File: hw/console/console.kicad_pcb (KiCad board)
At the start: 2 copper layers, 156 x 74 mm, 161 parts, among them J1 Batt, J301 USB-C 16P, J401 DM3AT-SF-PEJM5, J501 SPK 8R, J601 FFC-40 0.5mm, J901 UART, Q601 AO3400A, SW1 Движок, SW101 UP, SW102 DOWN, SW103 LEFT, SW104 RIGHT, SW105 SELECT, SW106 START, SW107 A, SW108 B, SW109 C, SW110 D, U1 F133-A, U2 SY8089AAAC, U3 SY8089AAAC, U4 SY8089AAAC, U401 W25Q32JVSSIQ, U5 TP4056, U501 PAM8301, Y1 24 МГц, Y2 32.768 кГц

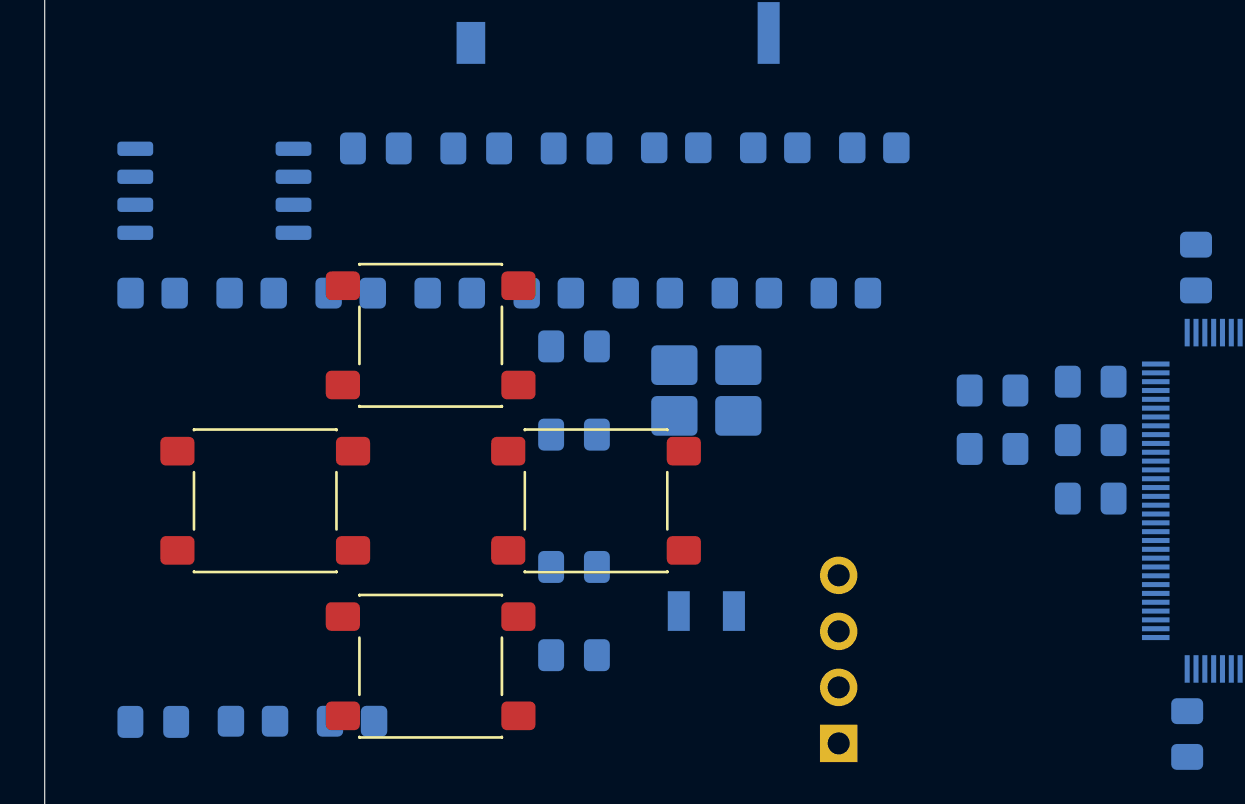
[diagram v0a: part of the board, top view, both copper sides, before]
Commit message: hw: осмотр платы глазами — флешка и кварцы стояли у края, а не у своих выводов
Проверки давали ноль, картинка — нет. Свободный карман вплотную к левому
торцу корпуса никто не занял, и обе детали, которым положено быть ближе всех,
оказались у самого края платы:

  U401 SPI NOR — 40 мм до выводов 14…19, хотя рядом с ними было пусто;
  Y1 24 МГц и Y2 32.768 кГц — по 20 мм до выводов 21…25.

Причина в том, что кольцо развязки занимает на левой стороне y = 32…36 в двух
рядах, а раскладчик по зонам просто ставил детали в свою зону у края. Теперь
U401 сидит в кармане y = 37…43 прямо у корпуса, кварцы — напротив своих
выводов за кольцом. Приоритет у развязки: петля тока по питанию важнее длины
кварцевой дорожки, а 24 МГц спокойно терпит десяток миллиметров.

Проверка на кварцы это пропускала, потому что порог «далеко» я поставил 25 мм
с потолка — при том, что вся левая сторона корпуса 12 мм в длину. Порог 12,
и заведена такая же проверка для флешки. Проверок стало восемнадцать.

Заодно 05-audio.md §7.5.1: выход класса D фильтрлесс, между усилителем и
динамиком катушек нет, и пара OUT+/OUT- — самый шумный узел платы. Требование
на разводку записано: вести парой, одинаковой длины, ничего чувствительного
рядом; если станет тесно — двигать U501 к разъёму, а не растягивать пару.

18 проверок платы — ноль, DRC кроме неразведённого — ноль, конвейер
идемпотентен, схема ERC ноль и audit.py ноль.

Co-Authored-By: Claude Opus 5 <noreply@anthropic.com>
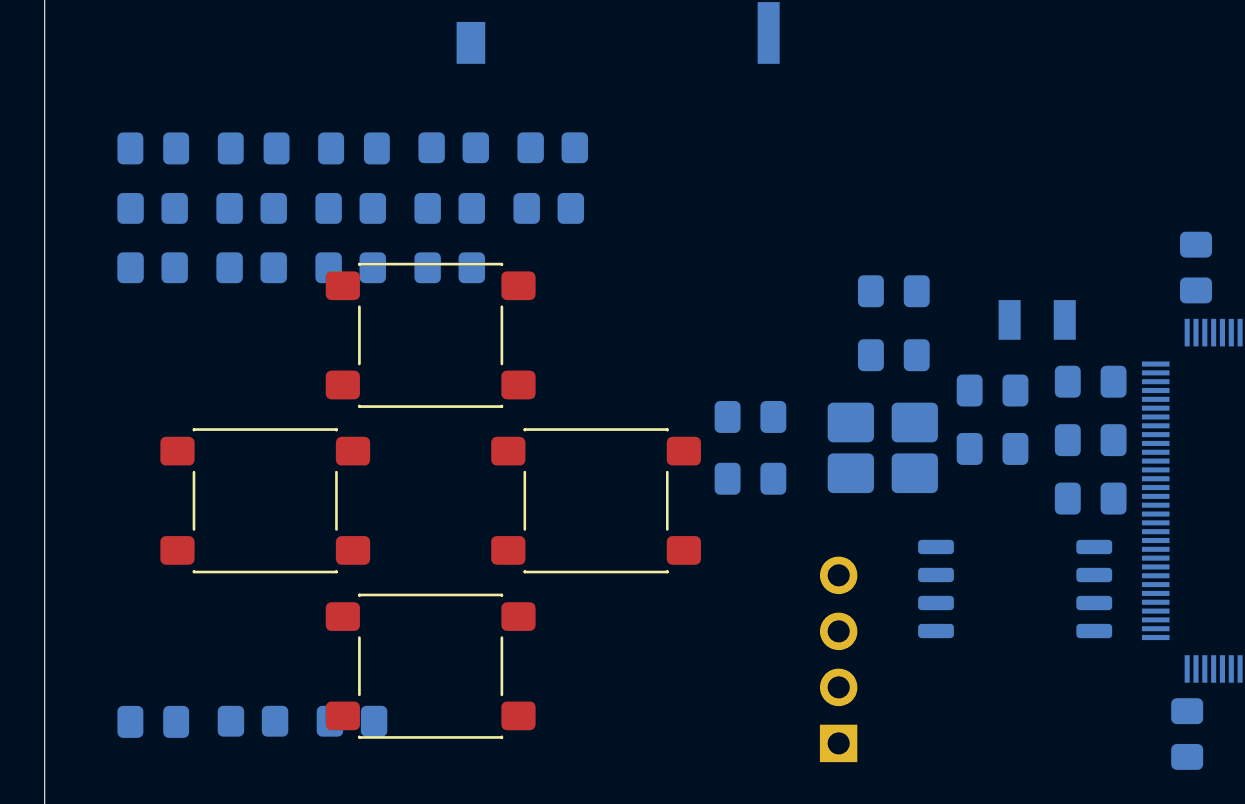
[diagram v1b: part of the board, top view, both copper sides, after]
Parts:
- moved U401 40.5 mm to (94.0, 81.0)
- moved R403 32.8 mm to (54.9, 63.7)
- moved Y2 20.0 mm to (95.0, 68.8)
- moved C18 19.9 mm to (88.5, 70.4)
- moved C17 19.1 mm to (88.5, 67.5)
- moved R411 18.0 mm to (68.4, 66.4)
- moved R408 18.0 mm to (54.9, 66.4)
- moved R409 18.0 mm to (59.4, 66.4)
- moved R410 18.0 mm to (63.9, 66.4)
- moved C401 10.1 mm to (54.9, 61.0)
- moved R401 10.1 mm to (68.5, 61.0)
- moved R402 10.1 mm to (73.0, 61.0)
- moved C402 10.1 mm to (59.5, 61.0)
- moved C403 10.1 mm to (64.0, 61.0)
- moved C15 8.62 mm to (82.0, 73.2)
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
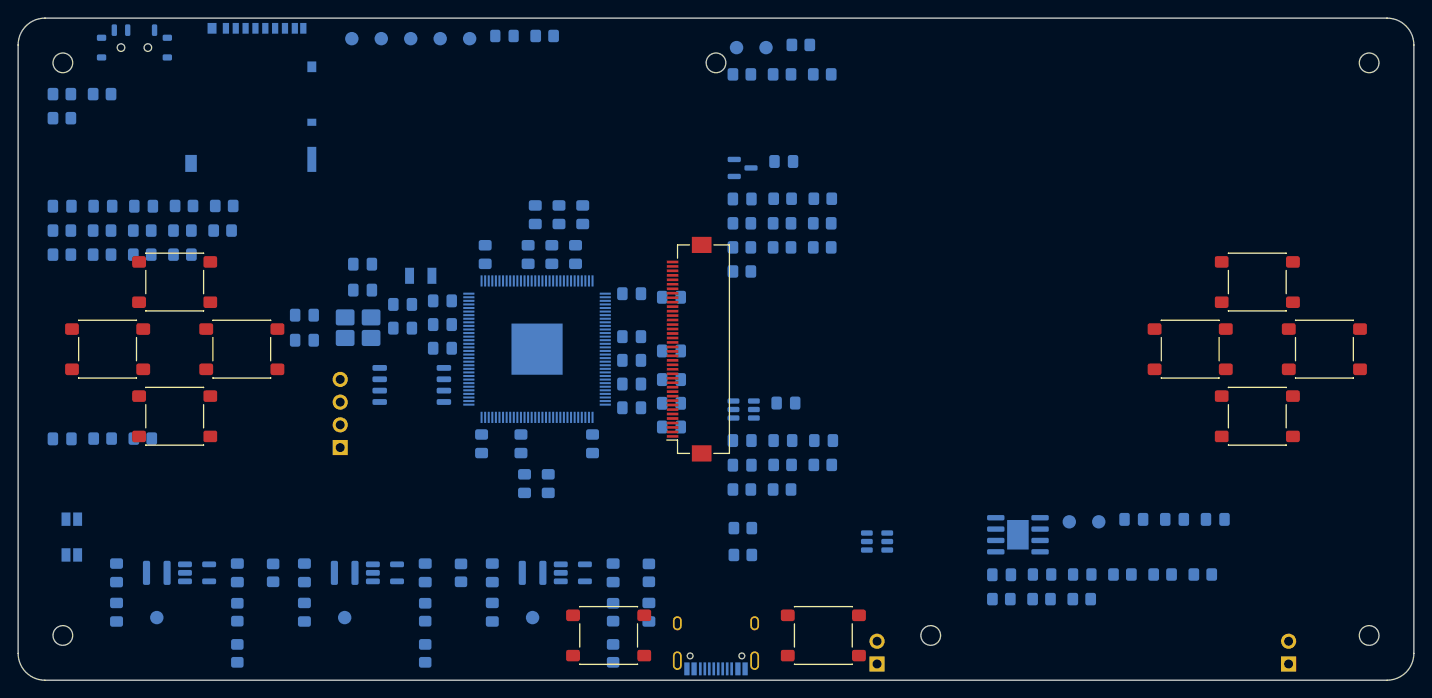
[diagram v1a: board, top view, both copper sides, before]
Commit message: hw: вариант C — все детали на лице, изнанка отдана банке
Andrey заметил то, что я проглядел: разъём шлейфа стоял на лице, а F133 на
изнанке. Посчитал по плате — 36 цепей требовали перехода через слой, и все в
самом тесном месте: шаг площадок разъёма 0.5 мм, наша переходная с зазором
даёт 1.1, сорок штук в ряд заняли бы 44 мм при ширине разъёма 19.5. То есть
три ряда веером и 36 заклёпок из проволоки вручную.

Мой довод против прорези («режет там, где идёт шина») был к тому же неверен:
если разъём стоит вплотную к прорези, а чип дальше, шина её вовсе не касается.
Я отверг прорезь по несуществующей причине и не взвесил, чем плачу.

Выход нашёлся не в прорези, а в том, чтобы поднять панель. Просвет 1.4 мм брался
из расчёта «под стеклом только разъём высотой 1.0». При 2.0 туда влезает всё:
F133 1.55, TP4056 1.75, дроссели 1.5, керамика 0.9. Все 155 деталей уехали на
лицо, на изнанке осталась одна банка.

Что это дало: монтаж в один проход, ноль переходных для шины дисплея, прорезь
не нужна, кнопки почти вровень со стеклом (0.15 мм против 0.75). Общая толщина
не выросла. Чем платим: под стеклом ничего не потрогать, для переделки панель
придётся снимать, между её изнанкой и деталями нужна плёнка.

F133 развёрнут на 180° и стоит правее разъёма — так шина `PD` смотрит прямо на
него. Заодно питание и USB ушли вниз, к нижнему торцу, хранение и такт вправо.

Круг «проверка — скриншот — правка» прошёл четыре раза. Проверки давали ноль,
картинка находила: USBLC6 сбоку от розетки вместо разрыва пары D+/D-; зарядник
в противоположном углу от USB и банки, обе цепи по 90 мм при 1 А; светодиоды
заряда на лице под правой ладонью; дисплейный блок по другую сторону разъёма
от корпуса. Всё перечислено в 10-mech.md §9.1.

18 проверок платы — ноль, DRC кроме неразведённого — ноль, конвейер из семи
шагов идемпотентен, схема ERC ноль и audit.py ноль.

Co-Authored-By: Claude Opus 5 <noreply@anthropic.com>
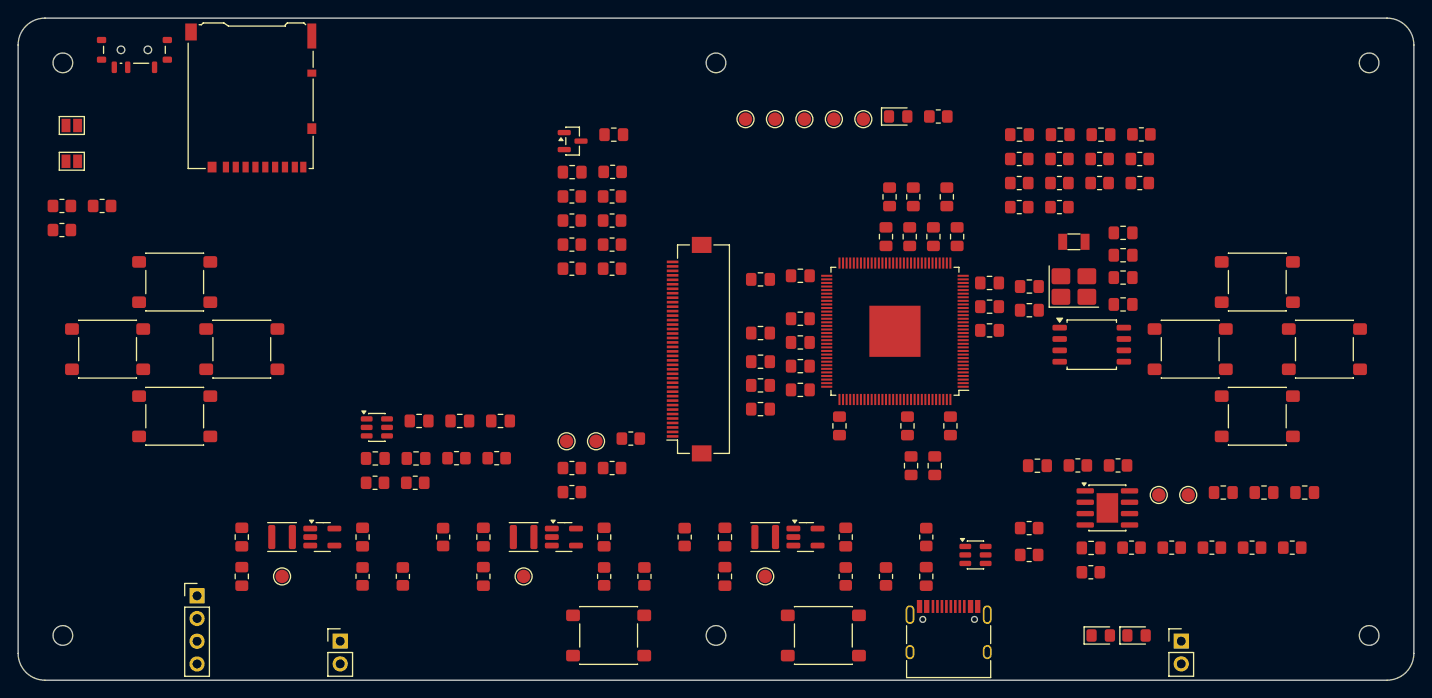
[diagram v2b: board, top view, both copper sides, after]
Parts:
- C1, C10, C11, C12, C13, C14, C15, C16, C17, C18, C19, C2, C3, C4, C401, C402, C403, C5, C501, C502, C503, C504, C505, C6, C601, C602, C7, C8, C801, C802, C803, C804, C805, C806, C807, C808, C809, C810, C811, C812, C813, C814, C815, C816, C817, C818, C819, C820, C821, C822, C823, C824, C825, C826, C827, C9, D1, D2, D301, D901, J1, J301, J401, J501, J901, JP1, JP301, L1, L2, L3, Q601, R1, R10, R11, R12, R13, R14, R15, R16, R17, R18, R19, R2, R20, R3, R301, R302, R4, R401, R402, R403, R404, R405, R406, R407, R408, R409, R410, R411, R5, R501, R502, R503, R504, R6, R601, R602, R603, R604, R605, R606, R607, R608, R609, R7, R8, R801, R802, R803, R804, R9, R901, SW1, TP1, TP2, TP3, TP4, TP5, TP801, TP802, TP901, TP902, TP903, TP904, TP905, U1, U2, U3, U4, U401, U5, U501, Y1, Y2: moved to F.Cu
- moved R408 116.3 mm to (170.9, 58.4)
- moved R409 116.3 mm to (175.4, 58.4)
- moved R404 111.8 mm to (170.9, 55.7)
- moved R403 111.8 mm to (166.4, 55.7)
- moved R405 111.8 mm to (175.4, 55.7)
- moved C19 109.0 mm to (163.9, 90.0)
- moved R19 109.0 mm to (168.4, 90.0)
- moved R20 109.0 mm to (172.9, 90.0)
- moved C401 107.3 mm to (161.9, 53.0)
- moved C402 107.3 mm to (166.5, 53.0)
- moved C403 107.3 mm to (171.0, 53.0)
- moved R401 107.3 mm to (175.5, 53.0)
- moved R410 98.2 mm to (161.9, 61.1)
- moved R411 98.2 mm to (166.4, 61.1)
- moved R406 93.7 mm to (161.9, 58.4)
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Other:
- board text added: "банка 60 x 45 x 3 — одна на всей изнанке"
- board text added: "панель 84.07 x 54.56, стекло на 2.0 над платой"
- board text removed: "банка 60 x 45 x 3 на изнанке — деталей не ставить"
- board text removed: "панель 84.07 x 54.56, стекло на 1.4 над платой"

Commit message: hw: конвейер разводки — заливки убиты из задания, иначе слоёв ноль
Заливка земли на обеих сторонах в выгрузке Specctra — это `(plane GND)` на всю
плату, то есть медь, занятая чужой цепью. Трассировщик оставался без слоёв
вовсе и упирался в сотню неразведённых связей из 270. Убрали обе — на том же
первом проходе разведено 206 связей против 116.

Порядок работ теперь обычный: сначала дорожки, потом заливка и сшивка вокруг
них. `pcb06_planes.py` научился обходить уже проложенные дорожки — меряет
расстояние до отрезка, а не до габаритного прямоугольника, иначе косая дорожка
съедает вдвое больше поля, чем занимает.

Заодно: переходная 0,9/0,5 вместо кикадовской 0,6/0,3 (сверло 0,3 негодно для
заклёпки из проволоки), зазор 185 мкм дорожка-площадка — без него из-под F133
с шагом 0,4 мм выйти нельзя вообще, и трассировщик честно отказывался.

Свой волновой трассировщик остался под номером 10 — добивать за freerouting
то, что тот не осилил.

Co-Authored-By: Claude Opus 5 <noreply@anthropic.com>
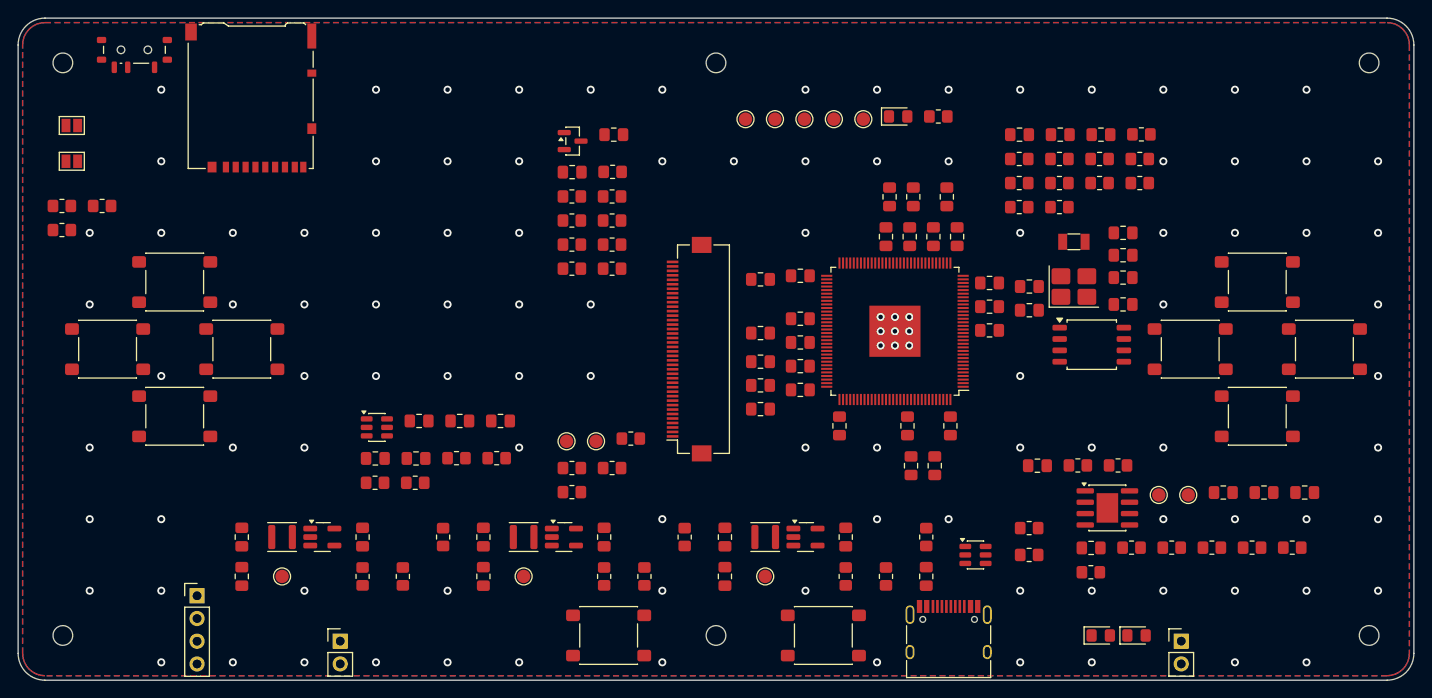
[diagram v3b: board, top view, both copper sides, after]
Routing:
- net GND: vias 0 -> 109
- added copper zone on B.Cu, net GND
- added copper zone on F.Cu, net GND

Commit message: hw: приём разводки — масштаб меряем, а не берём на веру
KiCad пишет `.dsn` в микрометрах, freerouting возвращает `.ses` в десятых
долях микрометра — при одинаковом заголовке `(resolution um 10)`. Разница
ровно вдесятеро: дорожки легли за плату, но на глаз выглядели складно, и
поймалось это только по числам.

Теперь масштаб не угадывается, а измеряется: в `.ses` есть посадка деталей,
их места мы знаем точно, отсюда множитель. Дадут разные — скрипт встанет.

Ещё по мелочи, всё найдено на живом прогоне:

* `pcb08_ses.py` снимает всю медь, а не всё кроме земли. Землю теперь разводит
  трассировщик, его переходные от наших заклёпок не отличить, и при повторном
  приёме те копились бы;
* заклёпки `pcb06` метит `SetLocked`, по этой метке их и снимает — чужие
  переходные разводки остаются на месте;
* `board.Remove()` в `pcb06` ломал всё, что создаётся после: `ZONE.Outline()`
  начинал отдавать сырой SwigPyObject. `RemoveNative` — не ломает.

Проверено целиком на коротком прогоне: 772 отрезка и 36 переходных легли, DRC
показывает ноль нарушений. Земля в остатке почти не встречается — заливка её
добирает; остаётся питание, оно расходится на два десятка конденсаторов.

Co-Authored-By: Claude Opus 5 <noreply@anthropic.com>
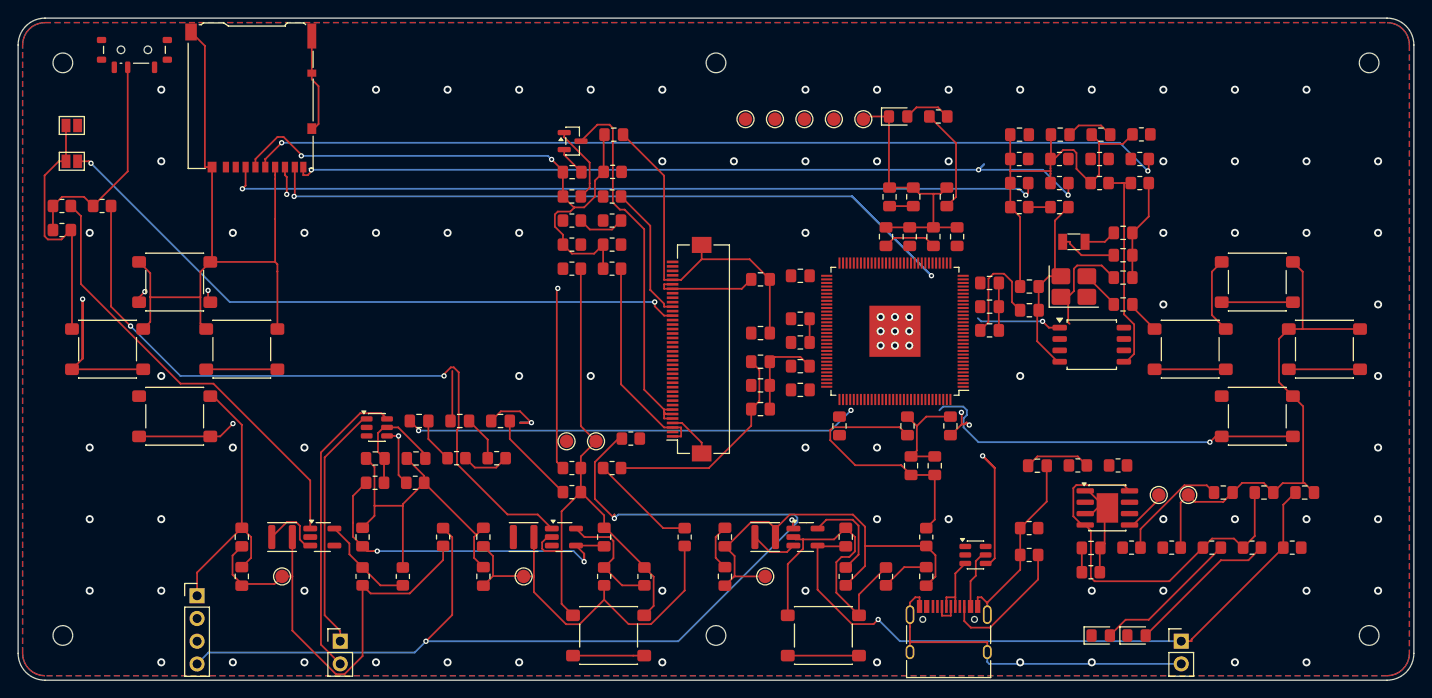
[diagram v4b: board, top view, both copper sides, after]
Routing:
- net GND: track 0.00 -> 569.2 mm, vias 109 -> 86
- net +3V3: track 0.00 -> 262.1 mm, vias 0 -> 6
- net VSYS: track 0.00 -> 123.2 mm, vias 0 -> 3
- net SDC0-D1: track 0.00 -> 103.7 mm, vias 0 -> 2
- net SD-CLK: track 0.00 -> 103.0 mm, vias 0 -> 2
- net SPI0-MOSI: track 0.00 -> 97.5 mm, vias 0 -> 2
- net SDC0-CMD: track 0.00 -> 91.9 mm, vias 0 -> 2
- net SDC0-DET: track 0.00 -> 91.0 mm, vias 0 -> 3
- net EN_1V8: track 0.00 -> 78.0 mm, vias 0 -> 2
- net Net-(C4-Pad1): track 0.00 -> 52.8 mm
- net HPOUTL: track 0.00 -> 50.9 mm, vias 0 -> 2
- net VBUS: track 0.00 -> 50.7 mm
- net EN_3V3: track 0.00 -> 49.3 mm
- net Net-(C10-Pad1): track 0.00 -> 47.5 mm
- net Net-(C5-Pad1): track 0.00 -> 44.8 mm
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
